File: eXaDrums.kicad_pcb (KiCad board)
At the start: 2 copper layers, 54.4 x 66.2 mm, 41 parts, among them J1 Conn_02x20_Odd_Even, J2 Conn_01x26_Female, J3 Conn_02x11_Odd_Even, U1 MCP3008, U2 ICL7660, U3 TLC274, U4 TLC274

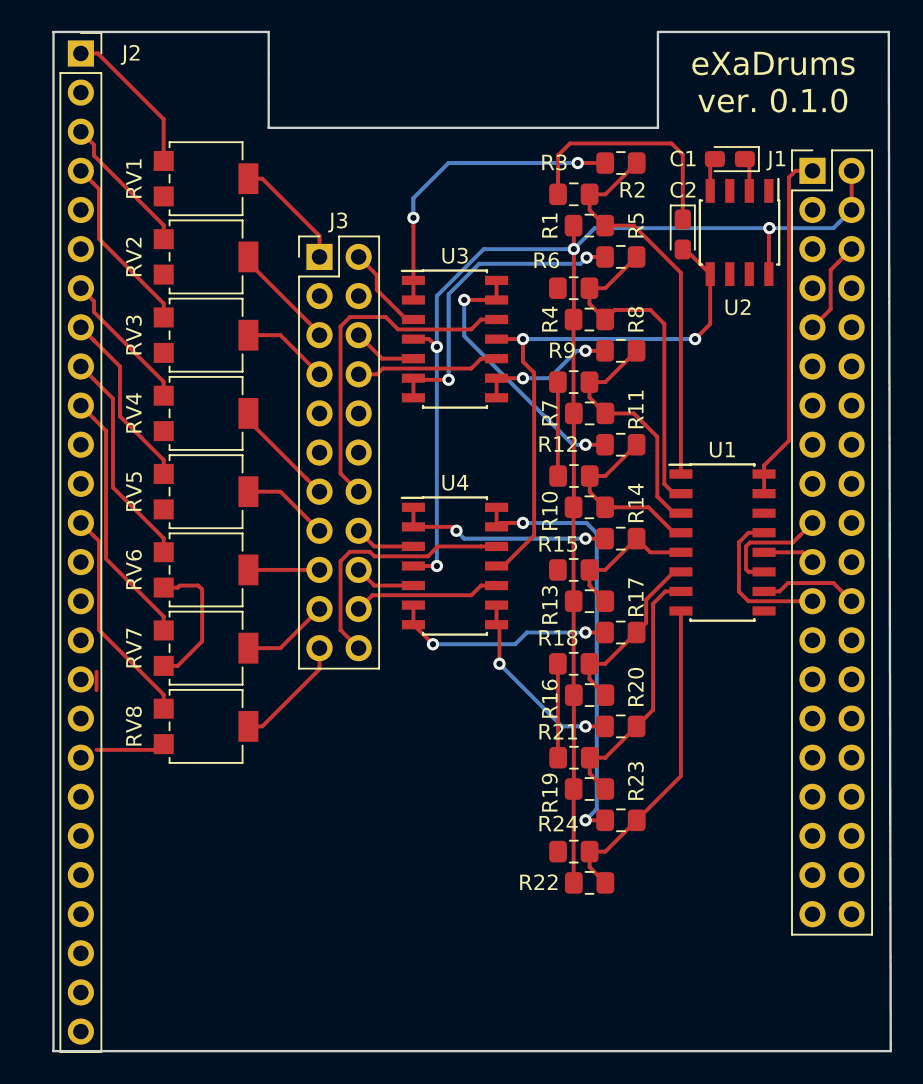
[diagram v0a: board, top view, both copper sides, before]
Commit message: Version 0.2.0: New board layout, and DB25 connector.
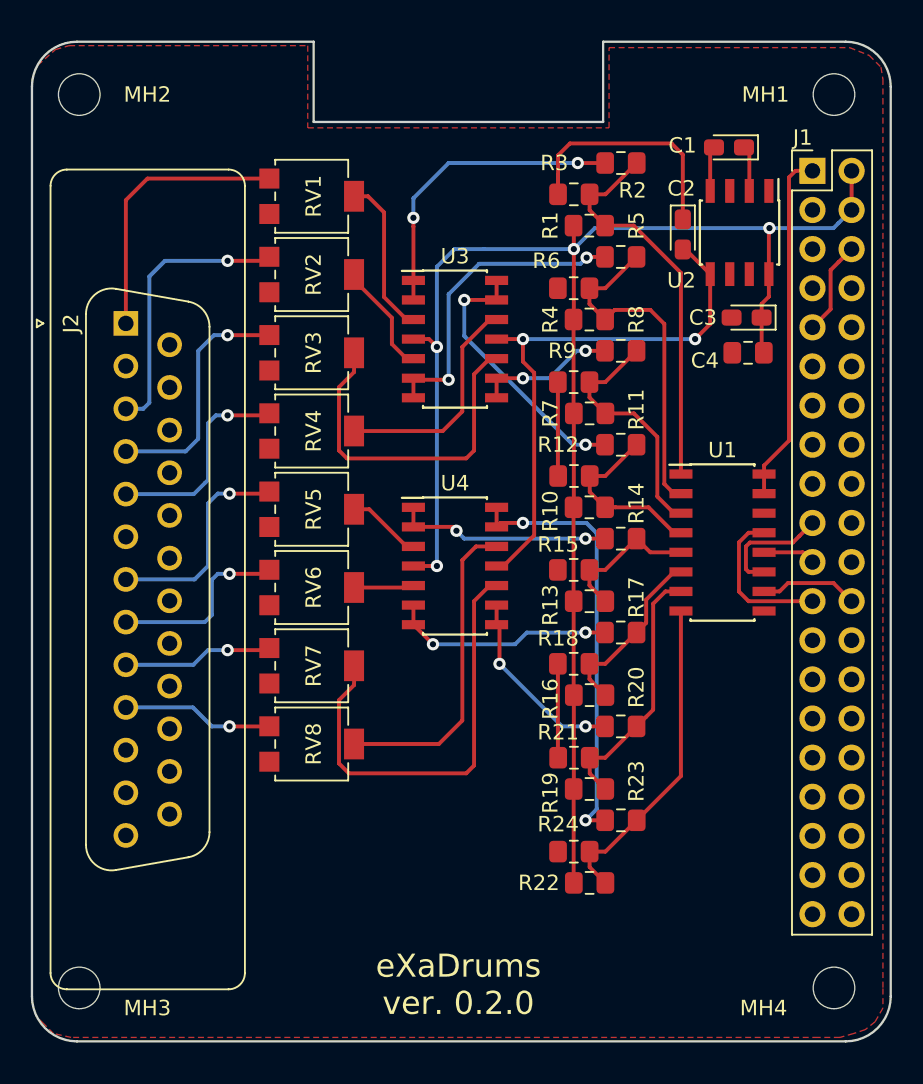
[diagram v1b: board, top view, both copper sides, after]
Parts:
- removed J3: Conn_02x11_Odd_Even, Connector_PinHeader_2.54mm:PinHeader_2x11_P2.54mm_Vertical
- added C3: 10uF, Capacitor_Tantalum_SMD:CP_EIA-2012-12_Kemet-R_Pad1.30x1.05mm_HandSolder, F.Cu at (163.1, 78.4)
- added C4: 220nF, Capacitor_SMD:C_0805_2012Metric_Pad1.15x1.40mm_HandSolder, F.Cu at (163.2, 80.6)
- added MH1: MountingHole, MountingHole:MountingHole_2.7mm_M2.5, F.Cu at (168.8, 63.9)
- added MH2: MountingHole, MountingHole:MountingHole_2.7mm_M2.5, F.Cu at (119.8, 63.9)
- added MH3: MountingHole, MountingHole:MountingHole_2.7mm_M2.5, F.Cu at (119.8, 121.9)
- added MH4: MountingHole, MountingHole:MountingHole_2.7mm_M2.5, F.Cu at (168.8, 121.9)
- J2: value Conn_01x26_Female -> DB25_Female; footprint Connector_PinSocket_2.54mm:PinSocket_1x26_P2.54mm_Vertical -> Connector_Dsub:DSUB-25_Female_Vertical_P2.77x2.84mm
- moved J2 17.8 mm to (122.8, 78.7), turned to 90 degrees
- moved RV1 6.95 mm to (134.9, 70.5)
- moved RV2 6.95 mm to (134.9, 75.6)
- moved RV3 6.95 mm to (134.9, 80.6)
- moved RV4 6.95 mm to (134.9, 85.7)
- moved RV5 6.95 mm to (134.9, 90.8)
- moved RV6 6.95 mm to (134.9, 95.9)
- moved RV7 6.95 mm to (134.9, 101.0)
- moved RV8 6.95 mm to (134.9, 106.0)
- moved C1 0.76 mm to (162.0, 67.3)
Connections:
- J2 pad 13: Net-(J2-Pad13) -> (no net)
- J2 pad 16: GND -> (no net)
- J2 pad 25: GND -> (no net)
- J2 pad 5: (no net) -> Net-(J2-Pad5)
- RV1 pad 2: Net-(J3-Pad1) -> Net-(RV1-Pad2)
- RV2 pad 2: Net-(J3-Pad5) -> Net-(RV2-Pad2)
- RV3 pad 2: Net-(J3-Pad7) -> Net-(RV3-Pad2)
- RV4 pad 1: Net-(J2-Pad7) -> Net-(J2-Pad5)
- RV4 pad 2: Net-(J3-Pad13) -> Net-(RV4-Pad2)
- RV5 pad 1: Net-(J2-Pad8) -> Net-(J2-Pad7)
- RV5 pad 2: Net-(J3-Pad15) -> Net-(RV5-Pad2)
- RV6 pad 1: Net-(J2-Pad9) -> Net-(J2-Pad8)
- RV6 pad 2: Net-(J3-Pad17) -> Net-(RV6-Pad2)
- RV7 pad 1: Net-(J2-Pad10) -> Net-(J2-Pad9)
- RV7 pad 2: Net-(J3-Pad19) -> Net-(RV7-Pad2)
- RV8 pad 1: Net-(J2-Pad13) -> Net-(J2-Pad10)
- RV8 pad 2: Net-(J3-Pad21) -> Net-(RV8-Pad2)
- U3 pad 10: Net-(J3-Pad8) -> Net-(RV3-Pad2)
- U3 pad 12: Net-(J3-Pad14) -> Net-(RV4-Pad2)
- U3 pad 3: Net-(J3-Pad2) -> Net-(RV1-Pad2)
- U3 pad 5: Net-(J3-Pad6) -> Net-(RV2-Pad2)
- U4 pad 10: Net-(J3-Pad20) -> Net-(RV7-Pad2)
- U4 pad 12: Net-(J3-Pad22) -> Net-(RV8-Pad2)
- U4 pad 3: Net-(J3-Pad16) -> Net-(RV5-Pad2)
- U4 pad 5: Net-(J3-Pad18) -> Net-(RV6-Pad2)
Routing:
- net Net-(RV7-Pad2): track 0.00 -> 28.5 mm
- net Net-(RV3-Pad2): track 0.00 -> 23.1 mm
- net Net-(J3-Pad14): track 22.2 -> 0.00 mm
- net Net-(RV8-Pad2): track 0.00 -> 20.7 mm
- net Net-(J3-Pad22): track 16.9 -> 0.00 mm
- net GND: track 50.0 -> 35.1 mm
- net Net-(RV4-Pad2): track 0.00 -> 14.7 mm
- net Net-(J2-Pad13): track 14.3 -> 0.00 mm
- net Net-(J2-Pad5): track 0.00 -> 13.6 mm, vias 0 -> 1
- net Net-(RV1-Pad2): track 0.00 -> 10.4 mm
- net Net-(J3-Pad20): track 9.59 -> 0.00 mm
- net Net-(J3-Pad8): track 9.38 -> 0.00 mm
- net Net-(J2-Pad3): track 9.21 -> 18.2 mm, vias 0 -> 1
- net Net-(J2-Pad1): track 9.85 -> 17.9 mm
- net Net-(J3-Pad21): track 7.52 -> 0.00 mm
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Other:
- board size 54.4 x 66.2 mm -> 55.8 x 64.9 mm
- board text added: "eXaDrums ver. 0.2.0"
- board text removed: "eXaDrums ver. 0.1.0"
